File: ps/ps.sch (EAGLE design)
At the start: 70 parts, among them IC1 LM675, Q1 NPN-D, Q2 NPN-D, U2 LM317, U3 TLC555CD, U4 LM317, U5 LM317

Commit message: PS rerouted
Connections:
- net VCC: now also C1.1, D4.A, Q2.C, R5.2, U1.IN
- net VINF: no longer C1.1, D4.A, Q2.C, R5.2, U1.IN
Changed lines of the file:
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@@
-</segment>
-<segment>
-<pinref part="C1" gate="G$1" pin="1"/>
-<wire x1="22.86" y1="73.66" x2="22.86" y2="76.2" width="0.1524" layer="91"/>
-<pinref part="U1" gate="G$1" pin="IN"/>
-<wire x1="22.86" y1="76.2" x2="26.67" y2="76.2" width="0.1524" layer="91"/>
-<wire x1="22.86" y1="76.2" x2="20.32" y2="76.2" width="0.1524" layer="91"/>
-<junction x="22.86" y="76.2"/>
-<label x="20.32" y="76.2" size="1.778" layer="95" rot="R180" xref="yes"/>
-</segment>
-<segment>
-<pinref part="D4" gate="G$1" pin="A"/>
-<pinref part="Q2" gate="G$1" pin="C"/>
-<wire x1="162.56" y1="106.68" x2="167.64" y2="106.68" width="0.1524" layer="91"/>
-<wire x1="162.56" y1="93.98" x2="162.56" y2="106.68" width="0.1524" layer="91"/>
-<pinref part="R5" gate="G$1" pin="2"/>
-<wire x1="144.78" y1="104.14" x2="144.78" y2="106.68" width="0.1524" layer="91"/>
-<wire x1="144.78" y1="106.68" x2="162.56" y2="106.68" width="0.1524" layer="91"/>
-<junction x="162.56" y="106.68"/>
-<wire x1="144.78" y1="106.68" x2="142.24" y2="106.68" width="0.1524" layer="91"/>
-<junction x="144.78" y="106.68"/>
-<label x="142.24" y="106.68" size="1.778" layer="95" rot="R180" xref="yes"/>
 </segment>
 <segment>
@@
 <pinref part="SUPPLY2" gate="G$1" pin="VCC"/>
 </segment>
+<segment>
+<pinref part="D4" gate="G$1" pin="A"/>
+<pinref part="Q2" gate="G$1" pin="C"/>
+<wire x1="162.56" y1="106.68" x2="167.64" y2="106.68" width="0.1524" layer="91"/>
+<wire x1="162.56" y1="93.98" x2="162.56" y2="106.68" width="0.1524" layer="91"/>
+<pinref part="R5" gate="G$1" pin="2"/>
+<wire x1="144.78" y1="104.14" x2="144.78" y2="106.68" width="0.1524" layer="91"/>
+<wire x1="144.78" y1="106.68" x2="162.56" y2="106.68" width="0.1524" layer="91"/>
+<junction x="162.56" y="106.68"/>
+<wire x1="144.78" y1="106.68" x2="142.24" y2="106.68" width="0.1524" layer="91"/>
+<junction x="144.78" y="106.68"/>
+<label x="142.24" y="106.68" size="1.778" layer="95" rot="R180" xref="yes"/>
+</segment>
+<segment>
+<pinref part="C1" gate="G$1" pin="1"/>
+<wire x1="22.86" y1="73.66" x2="22.86" y2="76.2" width="0.1524" layer="91"/>
+<pinref part="U1" gate="G$1" pin="IN"/>
+<wire x1="22.86" y1="76.2" x2="26.67" y2="76.2" width="0.1524" layer="91"/>
+<wire x1="22.86" y1="76.2" x2="20.32" y2="76.2" width="0.1524" layer="91"/>
+<junction x="22.86" y="76.2"/>
+<label x="20.32" y="76.2" size="1.778" layer="95" rot="R180" xref="yes"/>
+</segment>
 </net>

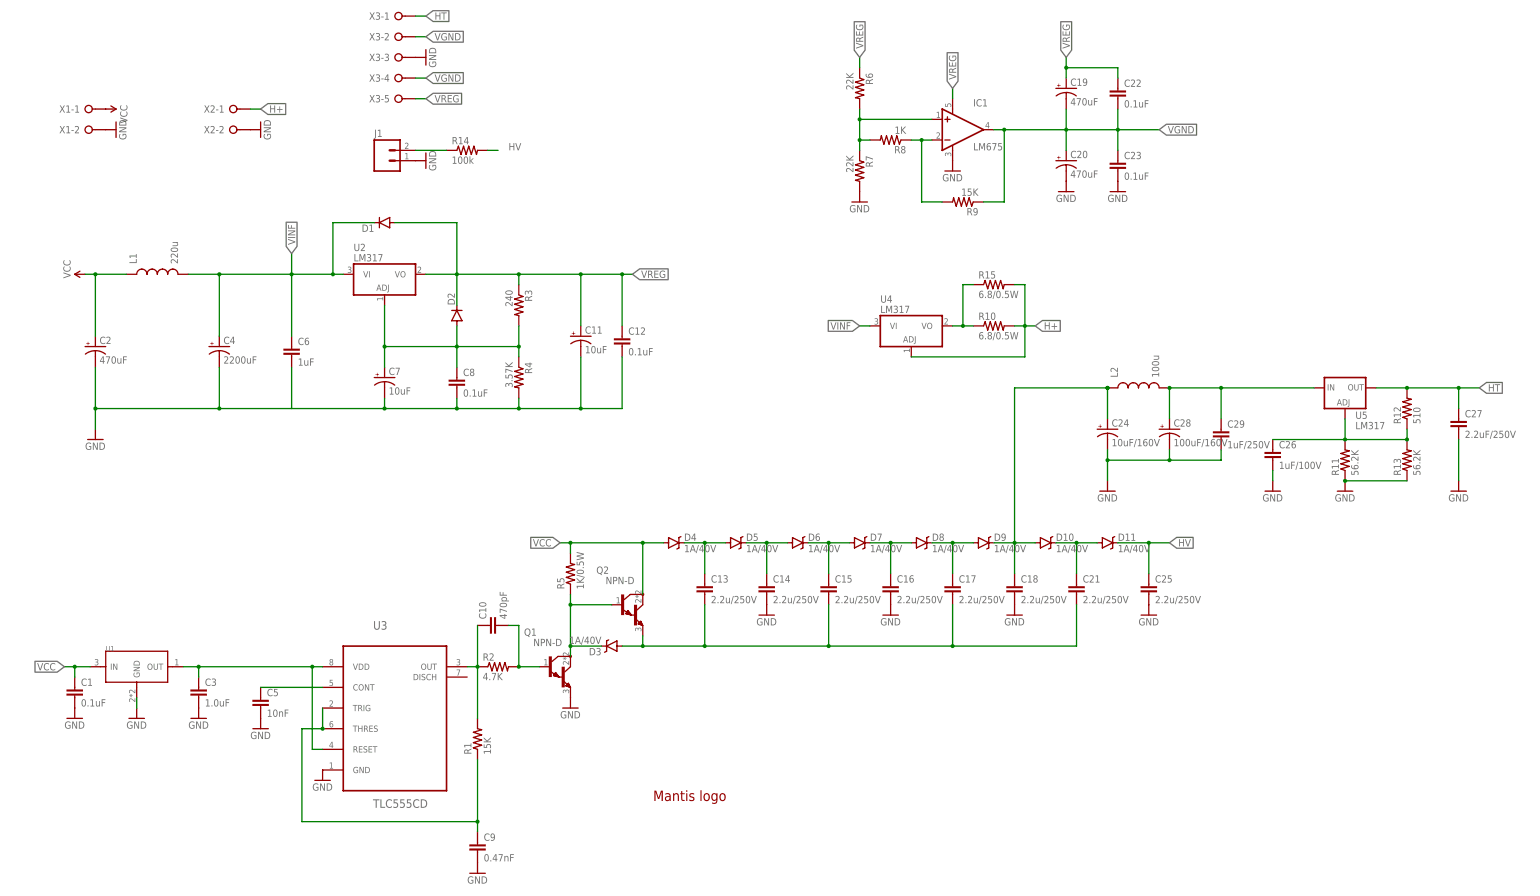
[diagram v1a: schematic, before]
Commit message: Separated grounds
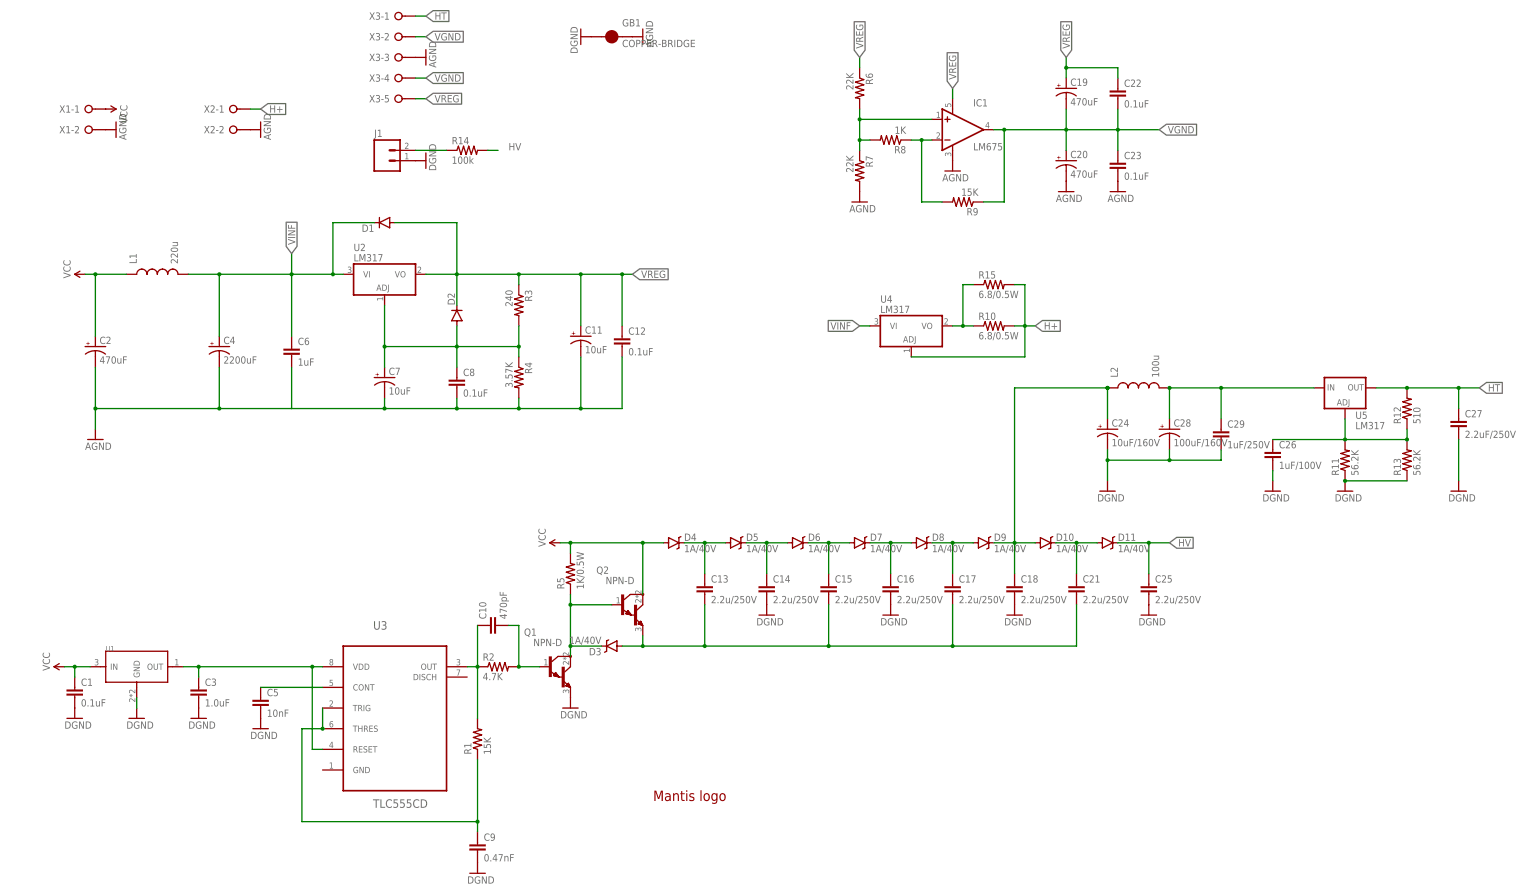
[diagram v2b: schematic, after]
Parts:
- added GB1: COPPER-BRIDGE, my:COPPER-BRIDGE
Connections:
- new net AGND: C11.-, C12.2, C2.-, C20.-, C23.2, C4.-, C6.2, C7.-, C8.2, GB1.2, IC1.V-, R4.2, R7.2, X1-2.KL, X2-2.KL, X3-3.KL
- net GND: now also GB1.1; no longer C11.-, C12.2, C2.-, C20.-, C23.2, C4.-, C6.2, C7.-, C8.2, IC1.V-, R4.2, R7.2, U3.GND, X1-2.KL, X2-2.KL, X3-3.KL

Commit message: More tweaks
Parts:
- J1: value (none) -> NE-2
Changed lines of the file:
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@@
 <part name="R10" library="SparkFun-Resistors" deviceset="RESISTOR" device="PTH-1/2W" value="6.8/0.5W"/>
 <part name="U4" library="my" deviceset="LM317" device=""/>
-<part name="J1" library="SparkFun-Connectors" deviceset="M02" device="PTH"/>
+<part name="J1" library="SparkFun-Connectors" deviceset="M02" device="PTH" value="NE-2"/>
 <part name="R14" library="SparkFun-Resistors" deviceset="100KOHM-1/10W-1%(0603)" device="" value="100k"/>
 <part name="R15" library="SparkFun-Resistors" deviceset="RESISTOR" device="PTH-1/2W" value="6.8/0.5W"/>

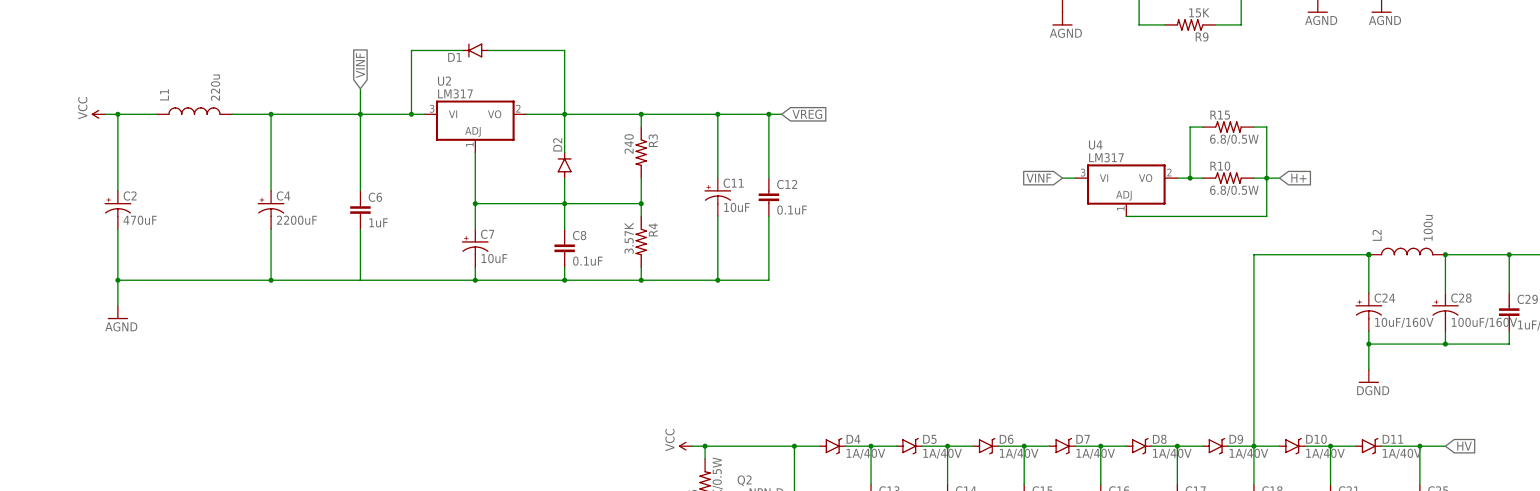
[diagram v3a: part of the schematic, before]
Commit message: LC damping resistors added to PS
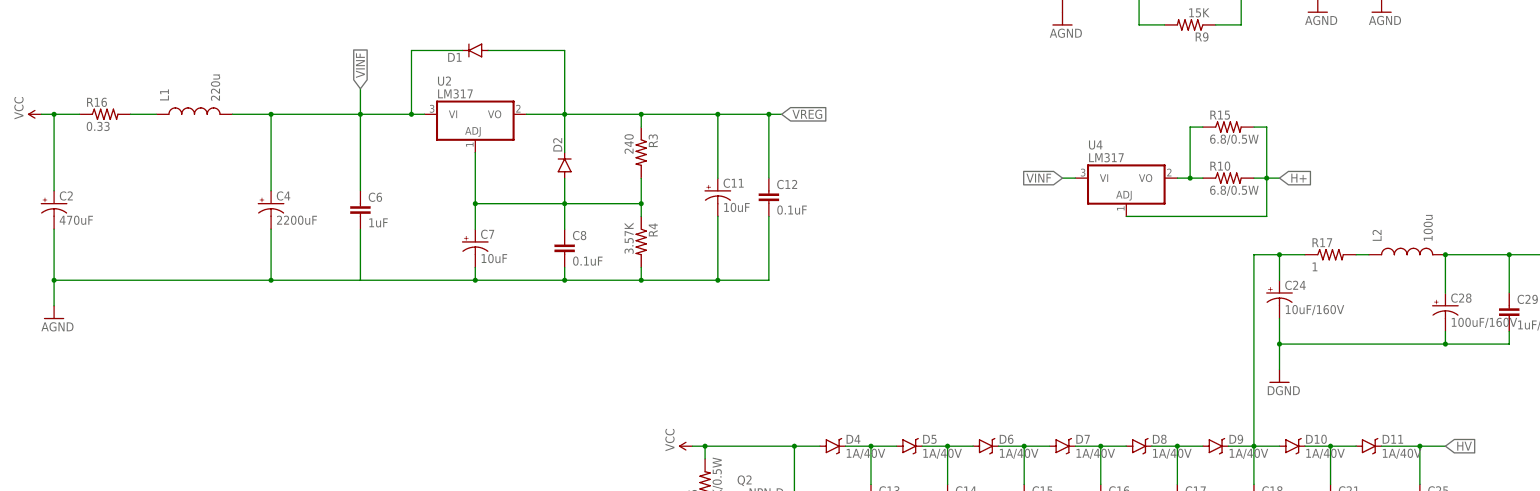
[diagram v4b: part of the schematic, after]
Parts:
- added R16: 0.33, SparkFun-Resistors:RESISTORPTH-1/4W
- added R17: 1, SparkFun-Resistors:RESISTORPTH-1/4W-VERT
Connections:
- new net N$16: L2.1, R17.2
- new net N$9: L1.1, R16.2
- net N$15: now also R17.1; no longer L2.1
- net VCC: now also R16.1; no longer L1.1
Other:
- moved on the sheet: C2, C24
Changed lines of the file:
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@@
 <part name="U$10" library="SparkFun-Aesthetics" deviceset="AGND" device=""/>
 <part name="GB1" library="my" deviceset="COPPER-BRIDGE" device=""/>
+<part name="R16" library="SparkFun-Resistors" deviceset="RESISTOR" device="PTH-1/4W" value="0.33"/>
+<part name="R17" library="SparkFun-Resistors" deviceset="RESISTOR" device="PTH-1/4W-VERT" value="1"/>
 </parts>
 <sheets>
@@
 <instance part="C18" gate="G$1" x="254" y="96.52"/>
 <instance part="C21" gate="G$1" x="269.24" y="96.52"/>
-<instance part="C24" gate="G$1" x="276.86" y="134.62"/>
+<instance part="C24" gate="G$1" x="259.08" y="137.16"/>
 <instance part="U5" gate="G$1" x="335.28" y="144.78"/>
 <instance part="C25" gate="G$1" x="287.02" y="96.52"/>
@@
 <instance part="C6" gate="G$1" x="76.2" y="152.4"/>
 <instance part="L1" gate="G$1" x="43.18" y="172.72" rot="R90"/>
-<instance part="C2" gate="G$1" x="27.94" y="154.94"/>
-<instance part="SUPPLY1" gate="G$1" x="25.4" y="172.72" rot="R90"/>
+<instance part="C2" gate="G$1" x="15.24" y="154.94"/>
+<instance part="SUPPLY1" gate="G$1" x="12.7" y="172.72" rot="R90"/>
 <instance part="C20" gate="G$1" x="266.7" y="200.66"/>
 <instance part="C19" gate="G$1" x="266.7" y="218.44"/>
@@
 <instance part="SUPPLY3" gate="G$1" x="142.24" y="106.68" rot="R90"/>
 <instance part="SUPPLY4" gate="G$1" x="20.32" y="76.2" rot="R90"/>
-<instance part="U$1" gate="G$1" x="27.94" y="132.08"/>
+<instance part="U$1" gate="G$1" x="15.24" y="132.08"/>
 <instance part="U$2" gate="G$1" x="215.9" y="190.5"/>
 <instance part="U$3" gate="G$1" x="266.7" y="193.04"/>
@@
 <instance part="GND9" gate="G$1" x="254" y="88.9"/>
 <instance part="GND10" gate="G$1" x="287.02" y="88.9"/>
-<instance part="GND11" gate="G$1" x="276.86" y="119.38"/>
+<instance part="GND11" gate="G$1" x="259.08" y="119.38"/>
 <instance part="GND12" gate="G$1" x="317.5" y="119.38"/>
 <instance part="GND13" gate="G$1" x="335.28" y="119.38"/>
@@
 <instance part="U$10" gate="G$1" x="162.56" y="231.14" rot="R90"/>
 <instance part="GB1" gate="G$1" x="154.94" y="231.14"/>
+<instance part="R16" gate="G$1" x="25.4" y="172.72"/>
+<instance part="R17" gate="G$1" x="269.24" y="144.78"/>
 </instances>
 <busses>
@@
 <segment>
 <pinref part="C24" gate="G$1" pin="-"/>
-<wire x1="276.86" y1="121.92" x2="276.86" y2="127" width="0.1524" layer="91"/>
+<wire x1="259.08" y1="121.92" x2="259.08" y2="127" width="0.1524" layer="91"/>
 <pinref part="C28" gate="G$1" pin="-"/>
-<wire x1="276.86" y1="127" x2="276.86" y2="129.54" width="0.1524" layer="91"/>
+<wire x1="259.08" y1="127" x2="259.08" y2="132.08" width="0.1524" layer="91"/>
 <wire x1="292.1" y1="129.54" x2="292.1" y2="127" width="0.1524" layer="91"/>
-<wire x1="292.1" y1="127" x2="276.86" y2="127" width="0.1524" layer="91"/>
-<junction x="276.86" y="127"/>
+<wire x1="292.1" y1="127" x2="259.08" y2="127" width="0.1524" layer="91"/>
+<junction x="259.08" y="127"/>
 <pinref part="C29" gate="G$1" pin="2"/>
 <wire x1="304.8" y1="129.54" x2="304.8" y2="127" width="0.1524" layer="91"/>
@@
 <junction x="254" y="106.68"/>
 <wire x1="254" y1="106.68" x2="254" y2="144.78" width="0.1524" layer="91"/>
-<wire x1="254" y1="144.78" x2="276.86" y2="144.78" width="0.1524" layer="91"/>
+<wire x1="254" y1="144.78" x2="259.08" y2="144.78" width="0.1524" layer="91"/>
 <pinref part="C24" gate="G$1" pin="+"/>
-<wire x1="276.86" y1="137.16" x2="276.86" y2="144.78" width="0.1524" layer="91"/>
-<junction x="276.86" y="144.78"/>
-<pinref part="L2" gate="G$1" pin="1"/>
-<junction x="276.86" y="144.78"/>
+<wire x1="259.08" y1="139.7" x2="259.08" y2="144.78" width="0.1524" layer="91"/>
+<pinref part="R17" gate="G$1" pin="1"/>
+<wire x1="264.16" y1="144.78" x2="259.08" y2="144.78" width="0.1524" layer="91"/>
+<junction x="259.08" y="144.78"/>
 </segment>
 </net>
@@
 <segment>
 <pinref part="C2" gate="G$1" pin="+"/>
-<wire x1="27.94" y1="157.48" x2="27.94" y2="172.72" width="0.1524" layer="91"/>
-<pinref part="L1" gate="G$1" pin="1"/>
-<wire x1="27.94" y1="172.72" x2="35.56" y2="172.72" width="0.1524" layer="91"/>
-<wire x1="27.94" y1="172.72" x2="25.4" y2="172.72" width="0.1524" layer="91"/>
-<junction x="27.94" y="172.72"/>
+<wire x1="15.24" y1="157.48" x2="15.24" y2="172.72" width="0.1524" layer="91"/>
+<wire x1="15.24" y1="172.72" x2="20.32" y2="172.72" width="0.1524" layer="91"/>
+<wire x1="15.24" y1="172.72" x2="12.7" y2="172.72" width="0.1524" layer="91"/>
+<junction x="15.24" y="172.72"/>
 <pinref part="SUPPLY1" gate="G$1" pin="VCC"/>
+<pinref part="R16" gate="G$1" pin="1"/>
 </segment>
 <segment>
@@
 <wire x1="58.42" y1="139.7" x2="76.2" y2="139.7" width="0.1524" layer="91"/>
 <pinref part="C2" gate="G$1" pin="-"/>
-<wire x1="27.94" y1="149.86" x2="27.94" y2="139.7" width="0.1524" layer="91"/>
-<wire x1="27.94" y1="139.7" x2="58.42" y2="139.7" width="0.1524" layer="91"/>
+<wire x1="15.24" y1="149.86" x2="15.24" y2="139.7" width="0.1524" layer="91"/>
+<wire x1="15.24" y1="139.7" x2="58.42" y2="139.7" width="0.1524" layer="91"/>
 <junction x="58.42" y="139.7"/>
-<wire x1="27.94" y1="139.7" x2="27.94" y2="134.62" width="0.1524" layer="91"/>
-<junction x="27.94" y="139.7"/>
+<wire x1="15.24" y1="139.7" x2="15.24" y2="134.62" width="0.1524" layer="91"/>
+<junction x="15.24" y="139.7"/>
 <pinref part="U$1" gate="G$1" pin="AGND"/>
 </segment>
@@
 </segment>
 </net>
+<net name="N$9" class="1">
+<segment>
+<pinref part="L1" gate="G$1" pin="1"/>
+<wire x1="30.48" y1="172.72" x2="35.56" y2="172.72" width="0.1524" layer="91"/>
+<pinref part="R16" gate="G$1" pin="2"/>
+</segment>
+</net>
+<net name="N$16" class="0">
+<segment>
+<pinref part="R17" gate="G$1" pin="2"/>
+<pinref part="L2" gate="G$1" pin="1"/>
+<wire x1="274.32" y1="144.78" x2="276.86" y2="144.78" width="0.1524" layer="91"/>
+</segment>
+</net>
